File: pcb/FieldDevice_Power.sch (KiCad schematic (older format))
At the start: 12 parts, among them U1 LM2621

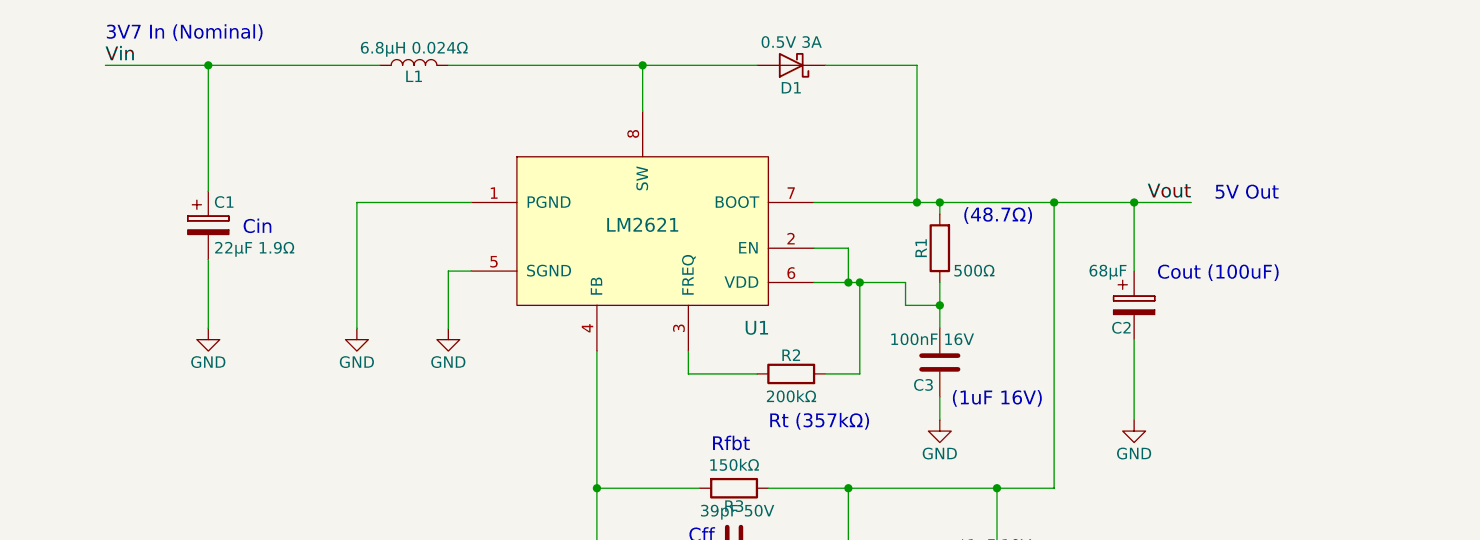
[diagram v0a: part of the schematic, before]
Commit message: Added the pin headers for Vin and Vout
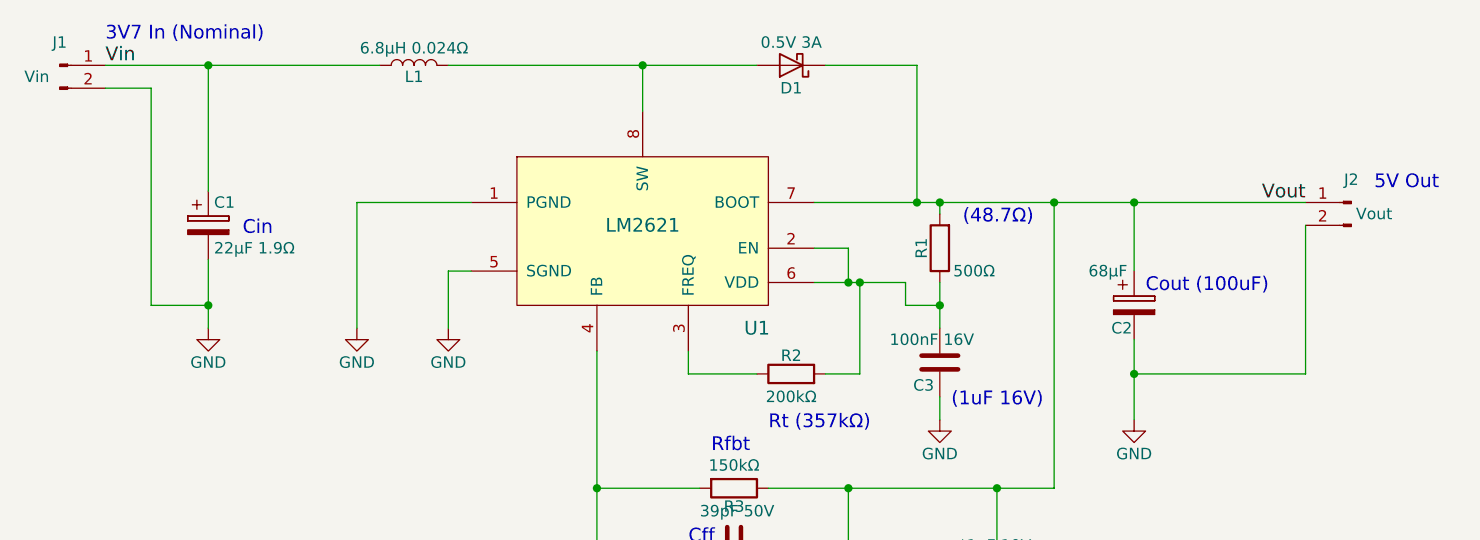
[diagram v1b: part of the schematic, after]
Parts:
- added J1: Vin, Pin_Headers:Pin_Header_Straight_1x02_Pitch2.54mm, symbol Conn_01x02_Male
- added J2: Vout, Pin_Headers:Pin_Header_Straight_1x02_Pitch2.54mm, symbol Conn_01x02_Male
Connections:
- net GND: now also J1.2 (Pin_2), J2.2 (Pin_2)
- net Vin: now also J1.1 (Pin_1)
- net Vout: now also J2.1 (Pin_1)
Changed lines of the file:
@@
 LIBS:contrib
 LIBS:valves
+LIBS:FieldDevice_Power-cache
 EELAYER 25 0
 EELAYER END
@@
 Connection ~ 5400 4100
 Wire Wire Line
-	6350 2600 8000 2600
+	6350 2600 8500 2600
 Wire Wire Line
 	6350 2800 6500 2800
@@
 Text Notes 5450 4650 0    60   ~ 0
 (49.9lΩ)
-Text Label 8000 2600 2    60   ~ 0
+Text Label 8500 2600 2    60   ~ 0
 Vout
 Connection ~ 3700 2000
 Text Label 3250 2000 0    60   ~ 0
 Vin
-Text Notes 7850 2950 0    60   ~ 0
+Text Notes 7800 3000 0    60   ~ 0
 Cout (100uF)
 $Comp
@@
 Text Notes 3850 2750 0    60   ~ 0
 Cin
-Text Notes 8100 2600 0    60   ~ 0
+Text Notes 8800 2550 0    60   ~ 0
 5V Out
 Text Notes 3250 1900 0    60   ~ 0
 3V7 In (Nominal)
+$Comp
+L Conn_01x02_Male J1
+U 1 1 59F89D18
+P 3050 2000
+F 0 "J1" H 3050 2100 50  0000 C CNN
+F 1 "Vin" H 2950 1950 50  0000 C CNN
+F 2 "Pin_Headers:Pin_Header_Straight_1x02_Pitch2.54mm" H 3050 2000 50  0001 C CNN
+F 3 "" H 3050 2000 50  0001 C CNN
+	1    3050 2000
+	1    0    0    -1
+$EndComp
+Wire Wire Line
+	3250 2100 3450 2100
+Wire Wire Line
+	3450 2100 3450 3050
+Wire Wire Line
+	3450 3050 3700 3050
+Connection ~ 3700 3050
+$Comp
+L Conn_01x02_Male J2
+U 1 1 59F89ECA
+P 8700 2600
+F 0 "J2" H 8700 2700 50  0000 C CNN
+F 1 "Vout" H 8600 2550 50  0000 C CNN
+F 2 "Pin_Headers:Pin_Header_Straight_1x02_Pitch2.54mm" H 8700 2600 50  0001 C CNN
+F 3 "" H 8700 2600 50  0001 C CNN
+	1    8700 2600
+	-1   0    0    -1
+$EndComp
+Wire Wire Line
+	8500 2700 8500 3350
+Wire Wire Line
+	8500 3350 7750 3350
+Connection ~ 7750 3350
 $EndSCHEMATC

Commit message: Completed the layout and parts decisions
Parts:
- added Tp1: VinTest, Pin_Headers:Pin_Header_Straight_1x02_Pitch2.54mm, symbol Conn_01x02_Male
- added Tp2: VoutTest, Pin_Headers:Pin_Header_Straight_1x02_Pitch2.54mm, symbol Conn_01x02_Male
- added Tp3: IinTest, Pin_Headers:Pin_Header_Straight_1x02_Pitch2.54mm, symbol Conn_01x02_Male
- added Tp4: IoutTest, Pin_Headers:Pin_Header_Straight_1x02_Pitch2.54mm, symbol Conn_01x02_Male
- C1: footprint FieldDevice_Power:Capacitor_1411 -> Capacitors_Tantalum_SMD:CP_Tantalum_Case-B_EIA-3528-21_Hand; Case Type (none) -> 3528-21 (Metric); Link Value -> https://www.digikey.de/scripts/DkSearch/dksus.dll?Detail&it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; MPN (none) -> 293D226X9016B2TE3
- C2: value 68μF -> 100μF; footprint FieldDevice_Power:Capacitor_2917 -> Capacitors_Tantalum_SMD:CP_Tantalum_Case-D_EIA-7343-31_Hand; Link Value -> https://www.digikey.de/scripts/DkSearch/dksus.dll?Detail&it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; MPN (none) -> 593D107X0010D2TE3
- C3: value 100nF 16V -> 1uF 16V; Link Value -> https://www.digikey.de/scripts/DkSearch/dksus.dll?Detail&it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; MPN (none) -> EMK212B7105KG-T
- C4: Link (none) -> https://www.digikey.de/scripts/DkSearch/dksus.dll?Detail&it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; MPN (none) -> CC0805JRNPO9BN390
- C5: Link (none) -> https://www.digikey.de/scripts/DkSearch/dksus.dll?Detail&it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; MPN (none) -> C0603C105Z8VACTU
- D1: Link (none) -> https://www.digikey.de/scripts/DkSearch/dksus.dll?Detail&it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; MPN (none) -> B320A-13-F
- L1: footprint FieldDevice_Power:INDUCTOR_VLS6045EX-6R8M -> FieldDevice_Power:INDUCTOR_1255AY-6R8M=P3; Link Value -> https://www.digikey.de/scripts/DkSearch/dksus.dll?Detail&it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; MPN (none) -> 1255AY-6R8M=P3
- R1: value 500Ω -> 48.7Ω; Link (none) -> https://www.digikey.de/scripts/DkSearch/dksus.dll?Detail&it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; MPN (none) -> CRCW040248R7FKED
- R2: value 200kΩ -> 357kΩ E96, 1%; Link (none) -> https://www.digikey.de/scripts/DkSearch/dksus.dll?Detail&it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; MPN (none) -> CRCW0402357KFKED
- R3: Link (none) -> https://www.digikey.de/scripts/DkSearch/dksus.dll?Detail&it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; MPN (none) -> RR1220P-154-D
- R4: value 50kΩ -> 49.9kΩ E96 1%; Link (none) -> https://www.digikey.de/scripts/DkSearch/dksus.dll?Detail&it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; MPN (none) -> CRCW040249K9FKED
- U1: Link (none) -> https://www.digikey.de/scripts/DkSearch/dksus.dll?Detail&it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; MPN (none) -> LM2621MM/NOPB
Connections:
- net GND: now also Tp1.2 (Pin_2), Tp2.2 (Pin_2)
- net Vin: now also Tp1.1 (Pin_1), Tp3.2 (Pin_2); no longer C1.1, L1.1
- net Vout: now also Tp2.1 (Pin_1), Tp4.1 (Pin_1); no longer C2.1, C4.1, C5.2, D1.1 (K), R1.2, R3.1, U1.7 (BOOT)
- new net Vin1: C1.1, L1.1, Tp3.1 (Pin_1)
- new net Vout1: C2.1, C4.1, C5.2, D1.1 (K), R1.2, R3.1, Tp4.2 (Pin_2), U1.7 (BOOT)
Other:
- note added: "(100nF 16V)"
- note added: "(500Ω)"
- note added: "Cout"
- note added: "Coutx"
- note added: "Rfbb (50kΩ)"
- note added: "Rt (200kΩ)"
- note removed: "(1uF 16V)"
- note removed: "(48.7Ω)"
- note removed: "(49.9lΩ)"
- note removed: "Cout (100uF)"
- note removed: "Coutx\n(*NOPOP)"
- note removed: "Rt (357kΩ)"
- moved on the sheet: C1, C2, C3, C4, C5, D1, J1, J2, L1, R1, R2, R3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

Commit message: Updated a replacement for R4
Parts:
- R4: Link https://www.digikey.de/scripts/DkSearch/dksus.dll?Detail&itemSeq=242528887&uq=636451075115136113 -> https://www.digikey.de/scripts/DkSearch/dksus.dll?Detail&itemSeq=242650584&uq=636451245580086657; MPN CRCW040249K9FKED -> RC0402FR-0749K9L
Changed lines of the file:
@@
 F 1 "49.9kΩ E96 1%" H 5000 5550 50  0000 C CNN
 F 2 "Resistors_SMD:R_0402" V 5280 5550 50  0001 C CNN
-F 3 "http://www.vishay.com/docs/20035/dcrcwe3.pdf" H 5350 5550 50  0001 C CNN
-F 4 "CRCW040249K9FKED" H 5350 5550 60  0001 C CNN "MPN"
-F 5 "https://www.digikey.de/scripts/DkSearch/dksus.dll?Detail&itemSeq=242528887&uq=636451075115136113" H 5350 5550 60  0001 C CNN "Link"
+F 3 "" H 5350 5550 50  0001 C CNN
+F 4 "RC0402FR-0749K9L" H 5350 5550 60  0001 C CNN "MPN"
+F 5 "https://www.digikey.de/scripts/DkSearch/dksus.dll?Detail&itemSeq=242650584&uq=636451245580086657" H 5350 5550 60  0001 C CNN "Link"
 	1    5350 5550
 	-1   0    0    1
